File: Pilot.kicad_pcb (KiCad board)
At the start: 4 copper layers, 204.5 x 158 mm, 113 parts, among them J1 Touchscreen, J10 Conn_01x02, J11 Conn_01x02, J12 Conn_01x02, J13 3.5'' LCD, J14 USB_B_Micro, J15 Conn_01x03, J16 Conn_01x03, J17 Conn_01x03, J18 Conn_01x03, J19 Conn_01x03, J2 Conn_01x02, J20 USB_B_Micro, J21 Conn_01x02, J3 Conn_01x02, J4 Conn_01x02, J5 Conn_01x02, J6 Conn_01x02, J7 Conn_01x02, J8 Conn_01x02, J9 Conn_01x02, SW1 SW_SPDT, SW2 SW_SPDT, SW3 SW_SPDT, SW4 SW_Wuerth_450301014042, U1 STM32F103CBT6, U2 W25X40CLSS, U3 AT24CS01-XHM, U4 USBLC6-2SC6, U5 STM32F103C8T6, U6 USBLC6-2SC6, U8 AMS1117-3.3, Y1 8MHz, Y2 8MHz

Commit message: rouch parts placement
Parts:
- added U9: ~, kwrzesni:SOT-25-5, F.Cu at (98.4, 28.8)
- moved U7 184.3 mm to (199.1, 52.3)
- moved J20 164.2 mm to (38.8, 15.2), turned to 180 degrees
- moved U4 162.0 mm to (210.5, 24.1), turned to -90 degrees
- moved U6 149.1 mm to (39.0, 21.5), turned to -90 degrees
- moved SW3 133.1 mm to (76.8, 17.0), turned to 180 degrees
- moved J14 131.0 mm to (210.7, 17.6), turned to 180 degrees
- moved SW1 128.1 mm to (194.1, 17.5), turned to 180 degrees
- moved J21 127.8 mm to (220.6, 117.8), turned to 90 degrees
- moved SW4 118.5 mm to (223.1, 88.3), turned to 90 degrees
- moved C12 109.3 mm to (212.4, 111.8), turned to 180 degrees
- moved Y2 107.4 mm to (47.6, 108.2), turned to 90 degrees
- moved C13 104.4 mm to (206.8, 112.0), turned to 180 degrees
- moved C16 103.4 mm to (209.7, 111.8), turned to 180 degrees
- moved R12 102.8 mm to (212.4, 112.9)
- moved C32 102.6 mm to (51.7, 106.3)
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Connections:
- U1 pad 22: unconnected-(U1-PB11-Pad22) -> FLASH_CS
- U1 pad 25: HOME_BUTTON -> BACK_BUTTON
- U1 pad 26: BACK_BUTTON -> PAGE_DOWN_BUTTON
- U1 pad 27: PAGE_DOWN_BUTTON -> PAGE_UP_BUTTON
- U1 pad 28: PAGE_UP_BUTTON -> HOME_BUTTON
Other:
- board size 204.5 x 158 mm -> 204.6 x 158 mm

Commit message: first wiring
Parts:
- removed the U9 at (105.2, 39.0)
- C10, C9: footprint Capacitor_SMD:C_0201_0603Metric -> Capacitor_SMD:C_0402_1005Metric
- C32, C33: footprint Capacitor_SMD:C_0603_1608Metric -> Capacitor_SMD:C_0402_1005Metric
- D1, D2: footprint Capacitor_SMD:C_0201_0603Metric -> Diode_SMD:D_0603_1608Metric
- R22, R23, R24, R25, R33: footprint Resistor_SMD:R_0201_0603Metric -> Resistor_SMD:R_0603_1608Metric
- moved C12 152.4 mm to (60.1, 117.9), turned to 90 degrees
- moved R12 150.3 mm to (62.2, 117.9), turned to -90 degrees
- moved C16 150.2 mm to (60.1, 125.8), turned to 90 degrees
- moved C13 148.3 mm to (60.1, 133.9), turned to 90 degrees
- moved R16 148.1 mm to (62.2, 125.8), turned to -90 degrees
- moved C14 147.0 mm to (60.1, 141.9), turned to 90 degrees
- moved R13 146.1 mm to (62.2, 133.9), turned to -90 degrees
- moved C15 145.2 mm to (60.1, 149.9), turned to 90 degrees
- moved R14 144.7 mm to (62.2, 141.9), turned to -90 degrees
- moved R15 142.9 mm to (62.2, 149.9), turned to -90 degrees
- moved R4 138.5 mm to (61.4, 93.1), turned to 90 degrees
- moved R10 101.2 mm to (126.6, 78.8)
- moved R11 98.4 mm to (103.2, 106.2)
- moved C11 98.3 mm to (103.2, 104.7)
- moved R26 95.3 mm to (156.5, 83.7), turned to 90 degrees
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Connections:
- C30 pad 1: +3.3VA -> +3.3VA_2
- C31 pad 1: +3.3VA -> +3.3VA_2
- C7 pad 1: +3.3VA -> +3.3VA_1
- C8 pad 1: +3.3VA -> +3.3VA_1
- L1 pad 2: +3.3VA -> +3.3VA_1
- L2 pad 2: +3.3VA -> +3.3VA_2
- U1 pad 10: UP_BUTTON -> MENU_BUTTON
- U1 pad 11: RIGHT_BUTTON -> HOME_BUTTON
- U1 pad 12: DOWN_BUTTON -> PAGE_UP_BUTTON
- U1 pad 13: LEFT_BUTTON -> PAGE_DOWN_BUTTON
- U1 pad 14: OK_BUTTON -> BACK_BUTTON
- U1 pad 25: BACK_BUTTON -> DOWN_BUTTON
- U1 pad 26: PAGE_DOWN_BUTTON -> RIGHT_BUTTON
- U1 pad 27: PAGE_UP_BUTTON -> OK_BUTTON
- U1 pad 28: HOME_BUTTON -> LEFT_BUTTON
- U1 pad 29: MENU_BUTTON -> UP_BUTTON
- U1 pad 9: +3.3VA -> +3.3VA_1
- U5 pad 9: +3.3VA -> +3.3VA_2
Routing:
- net GND: track 0.00 -> 164.0 mm, vias 0 -> 85
- net BATTERY_SCL: track 0.00 -> 141.5 mm, vias 0 -> 4
- net BATTERY_SDA: track 0.00 -> 136.7 mm, vias 0 -> 4
- net USART1_RX1: track 0.00 -> 130.5 mm
- net Net-(SW2-B): track 0.00 -> 128.1 mm, vias 0 -> 2
- net USART1_TX1: track 0.00 -> 122.5 mm
- net USB2_5V: track 0.00 -> 122.3 mm, vias 0 -> 2
- net BACK_BUTTON: track 0.00 -> 118.2 mm, vias 0 -> 2
- net PAGE_DOWN_BUTTON: track 0.00 -> 112.8 mm, vias 0 -> 2
- net HOME_BUTTON: track 0.00 -> 109.0 mm, vias 0 -> 2
- net +3.3V: track 0.00 -> 107.6 mm, vias 0 -> 79
- net PAGE_UP_BUTTON: track 0.00 -> 106.8 mm, vias 0 -> 2
- net MENU_BUTTON: track 0.00 -> 106.7 mm, vias 0 -> 2
- net RIGHT_GIMBAL_H: track 0.00 -> 102.6 mm, vias 0 -> 2
- net TOUCHSCREEN_RESET: track 0.00 -> 100.2 mm, vias 0 -> 2
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- added copper zone on F.Cu, net +3.3V
- added copper zone on In2.Cu, net +3.3V
- added copper zone on In1.Cu, net GND
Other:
- board size 204.6 x 158 mm -> 204 x 158 mm

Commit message: gerber files
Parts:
- SW4: value SW_Wuerth_450301014042 -> SW_SPDT
- moved R11 1.82 mm to (102.2, 104.7), turned to 180 degrees
- moved C11 1.78 mm to (102.2, 106.2), turned to 0 degrees
- moved J14 0.80 mm to (144.0, 2.80)
- moved J20 0.80 mm to (60.0, 2.80)
- moved SW4 0.30 mm to (201.7, 79.0)
- moved SW1 0.30 mm to (128.0, 2.30)
- moved SW2 0.30 mm to (2.30, 79.0)
- moved SW3 0.30 mm to (76.0, 2.30)
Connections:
- net +3.3VA_1 renamed 3.3VA_1
- net +3.3VA_2 renamed 3.3VA_2
- SW4 pad 1: BAT+ -> unconnected-(SW4-A-Pad1)
- SW4 pad 2: unconnected-(SW4-C-Pad2) -> GND
- SW4 pad 3: Net-(SW4-A) -> Net-(SW4-C)
- U7 pad 1: Net-(SW4-A) -> BAT+
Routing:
- net Net-(SW4-A): track 75.9 -> 0.00 mm
- net BAT+: track 17.8 -> 89.5 mm
- net Net-(SW4-C): track 0.00 -> 52.5 mm
- net GND: track 164.0 -> 173.7 mm, vias 85 -> 86
- net UP_BUTTON: track 62.0 -> 71.3 mm, vias 3 -> 2
- net LEFT_BUTTON: track 67.9 -> 73.1 mm
- net BAT-: track 96.3 -> 91.5 mm
- net ON_BUTTON: track 83.0 -> 79.5 mm
- net OK_BUTTON: track 69.9 -> 71.9 mm
- net +3.3V: track 107.6 -> 108.8 mm, vias 79 -> 80
- net USB1_5V: track 45.3 -> 46.3 mm
- net DOWN_BUTTON: track 82.6 -> 81.6 mm
- net USB2_5V: track 122.3 -> 123.1 mm
- net RIGHT_BUTTON: track 75.5 -> 74.7 mm
- net USB1_CONN+: track 4.87 -> 4.17 mm
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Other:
- outline, holes or cut-outs redrawn
- board text added: "+"
- board text added: "-"
- board text added: "BOOT"

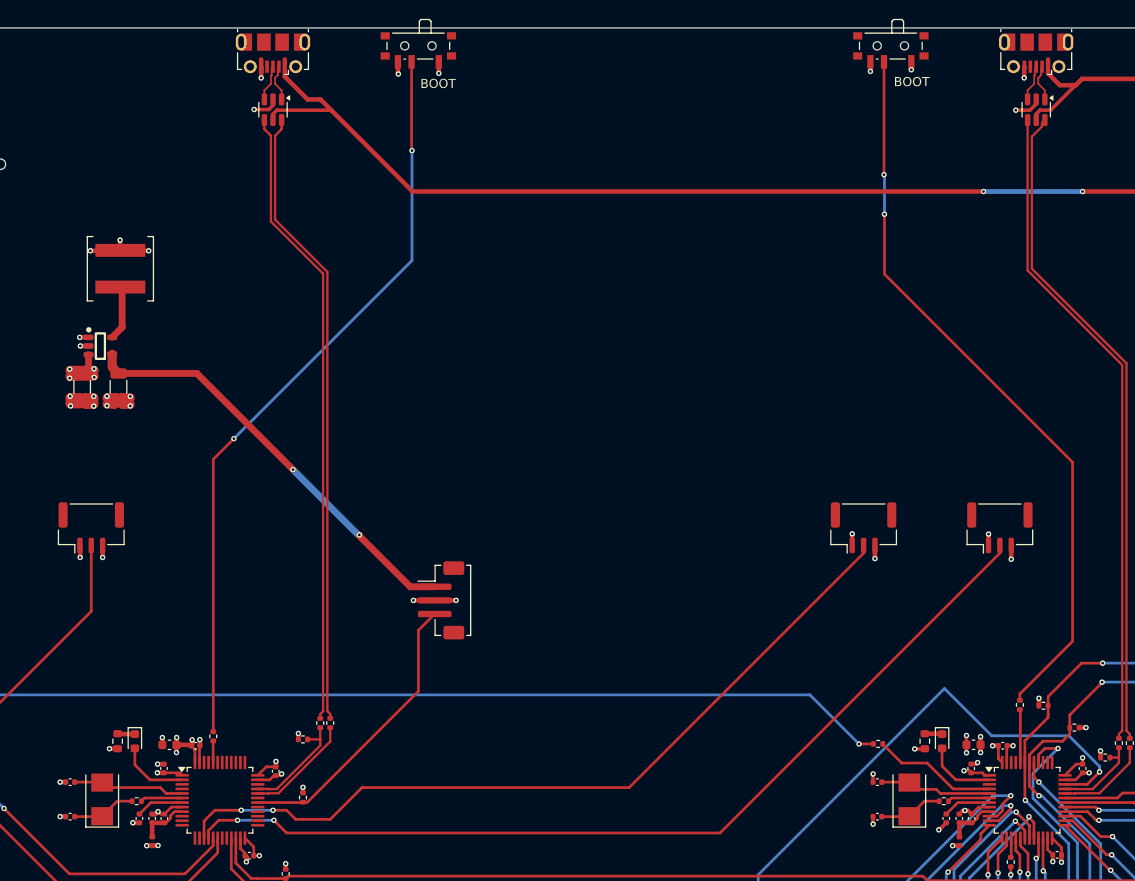
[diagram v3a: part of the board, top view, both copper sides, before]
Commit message: fix wrong footprints
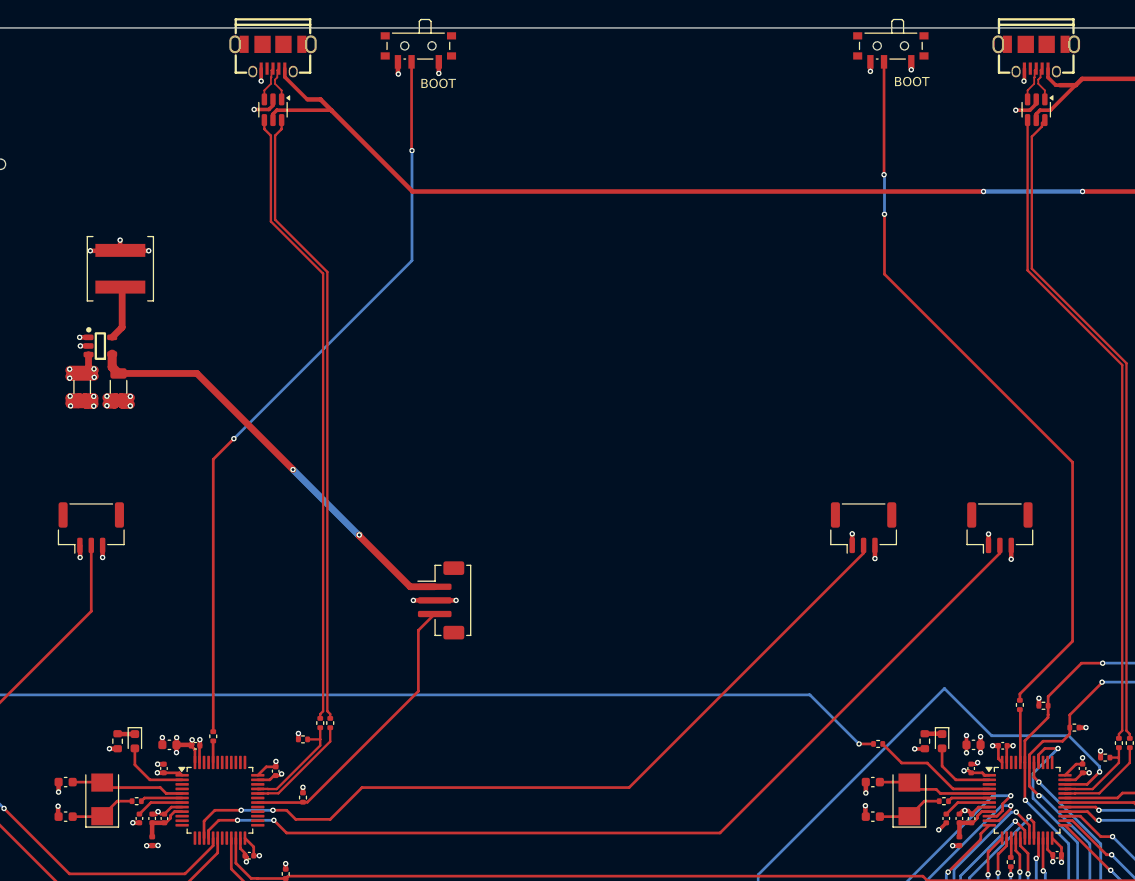
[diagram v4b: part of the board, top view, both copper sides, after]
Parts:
- C10, C32, C33, C9: footprint Capacitor_SMD:C_0402_1005Metric -> Capacitor_SMD:C_0603_1608Metric
- J14, J20: footprint Connector_USB:USB_Micro-B_Molex-105017-0001 -> kwrzesni:USB-B micro
- moved C10 0.50 mm to (126.0, 86.8)
- moved C32 0.50 mm to (37.2, 83.0)
- moved C33 0.50 mm to (37.2, 86.8)
- moved C9 0.50 mm to (126.0, 83.0)
- moved J14 0.50 mm to (144.0, 3.30)
- moved J20 0.50 mm to (60.0, 3.30)
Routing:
- net USB2_5V: track 123.1 -> 122.1 mm
- net USB1_5V: track 46.3 -> 45.6 mm
- net GND: track 173.7 -> 174.3 mm
